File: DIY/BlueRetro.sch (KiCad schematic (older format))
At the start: 4 parts, among them J2 Conn_01x19, J3 Conn_01x19, J5 PmodMicroSD, J6 DB25_Female

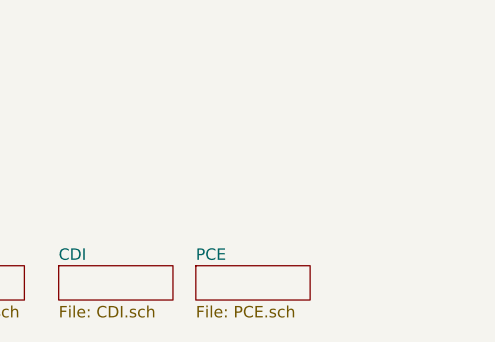
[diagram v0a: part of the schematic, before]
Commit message: [DIY] Add Jaguar adapter cable
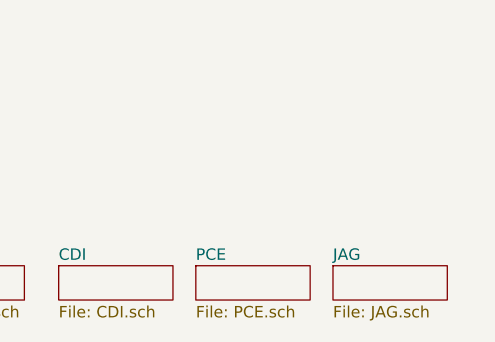
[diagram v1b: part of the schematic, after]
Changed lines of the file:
@@
 $Descr USLetter 11000 8500
 encoding utf-8
-Sheet 1 15
+Sheet 1 16
 Title "BlueRetro DIY"
 Date "2020-10-02"
@@
 F1 "PCE.sch" 50
 $EndSheet
+$Sheet
+S 9800 8700 500  150
+U 60BA3094
+F0 "JAG" 50
+F1 "JAG.sch" 50
+$EndSheet
 $EndSCHEMATC

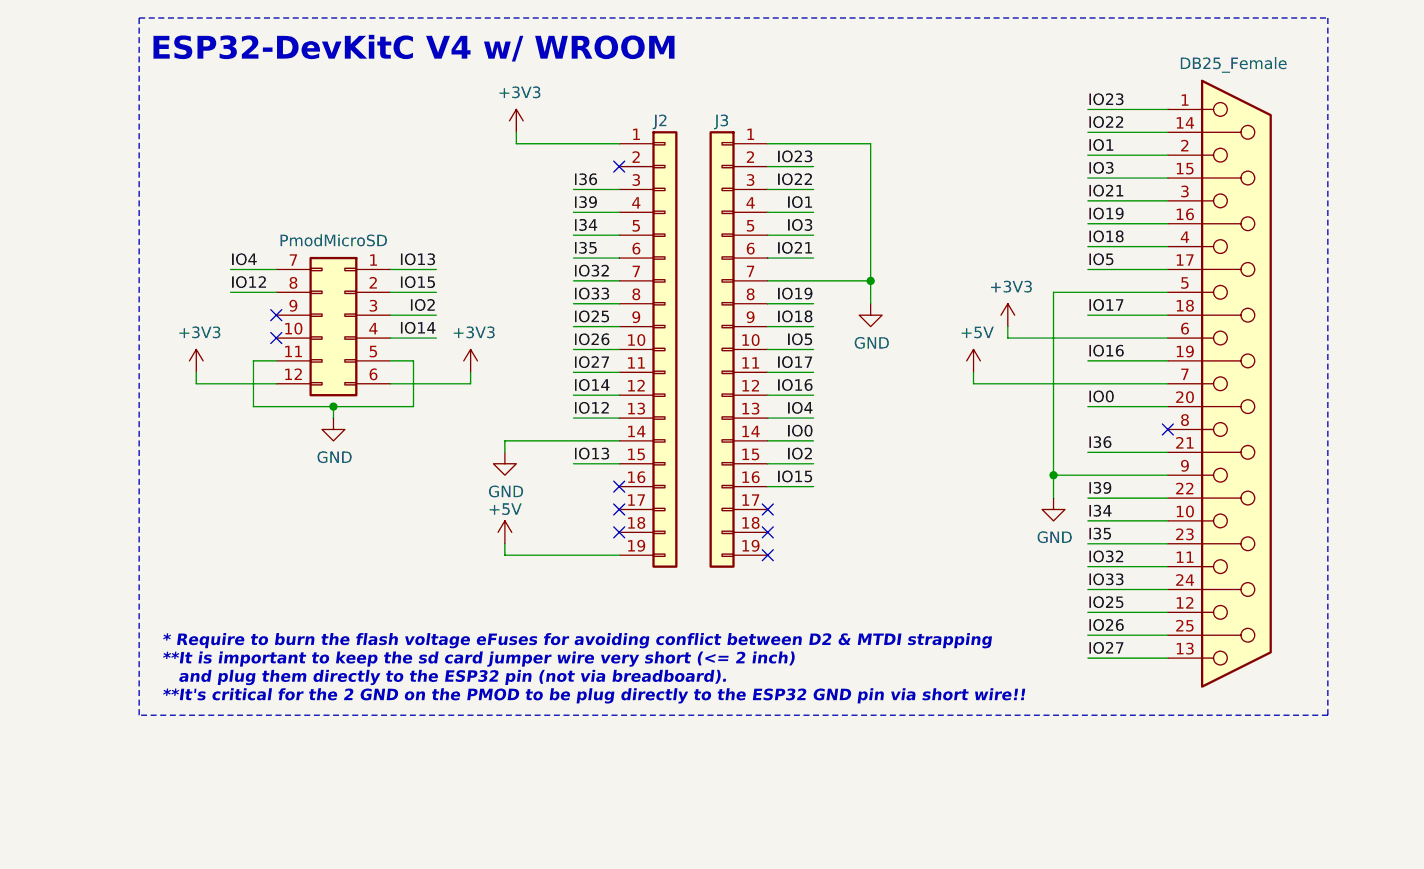
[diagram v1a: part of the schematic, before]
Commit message: [DIY] Remove sd card and add status LED
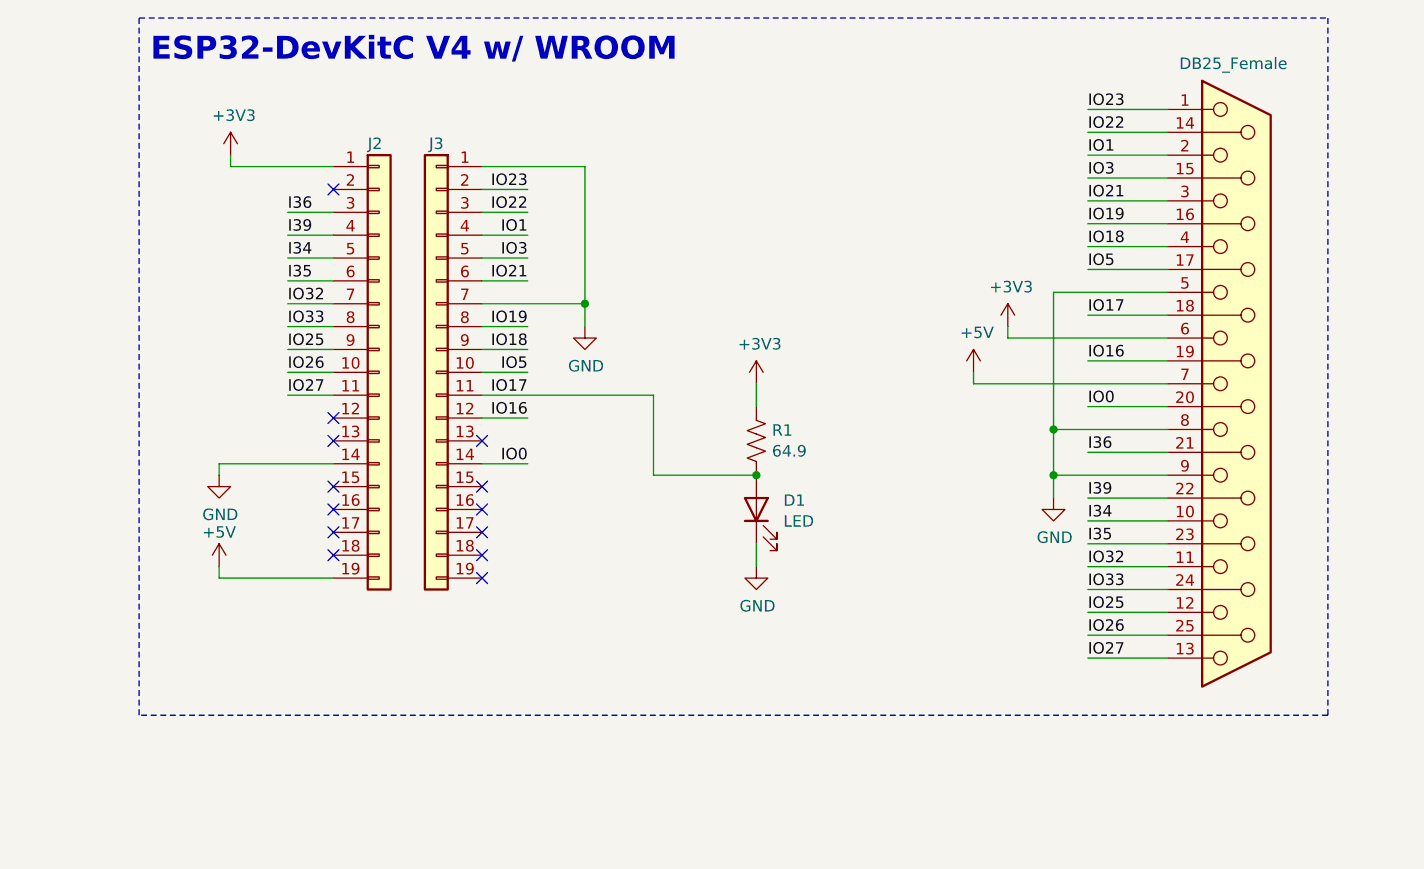
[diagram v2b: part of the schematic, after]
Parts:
- removed J5: PmodMicroSD, symbol Connector_Generic:Conn_02x06_Top_Bottom
- added D1: LED, symbol Device:LED
- added R1: 64.9, symbol Device:R_US
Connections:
- net +3V3: now also R1.1
- net GND: now also J6.8, D1.1 (K)
- net IO17: now also D1.2 (A), R1.2
- net IO12: no longer names the net of J2.13 (Pin_13)
- net IO13: no longer names the net of J2.15 (Pin_15)
- net IO14: no longer names the net of J2.12 (Pin_12)
- net IO15: no longer names the net of J3.16 (Pin_16)
- net IO2: no longer names the net of J3.15 (Pin_15)
- net IO4: no longer names the net of J3.13 (Pin_13)
- no-connect marks 10 -> 13
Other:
- note removed: "* Require to burn the flash voltage eFuses for avoiding conflict between D2 & MTDI strapping\n**It is important to keep the sd card jumper wire very short (<= 2 inch)\n and plug them directly to the ESP32 pin (not via breadboard).\n**It's critical for the 2 GND on the PMOD to be plug directly to the ESP32 GND pin via short wire!!"
- moved on the sheet: J2, J3
